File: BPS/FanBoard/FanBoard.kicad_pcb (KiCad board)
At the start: 2 copper layers, 45.1 x 33 mm, 21 parts, among them Q1 BUK9M34-100EX, Q2 BUK9M34-100EX, Q3 BUK9M34-100EX, Q4 BUK9M34-100EX

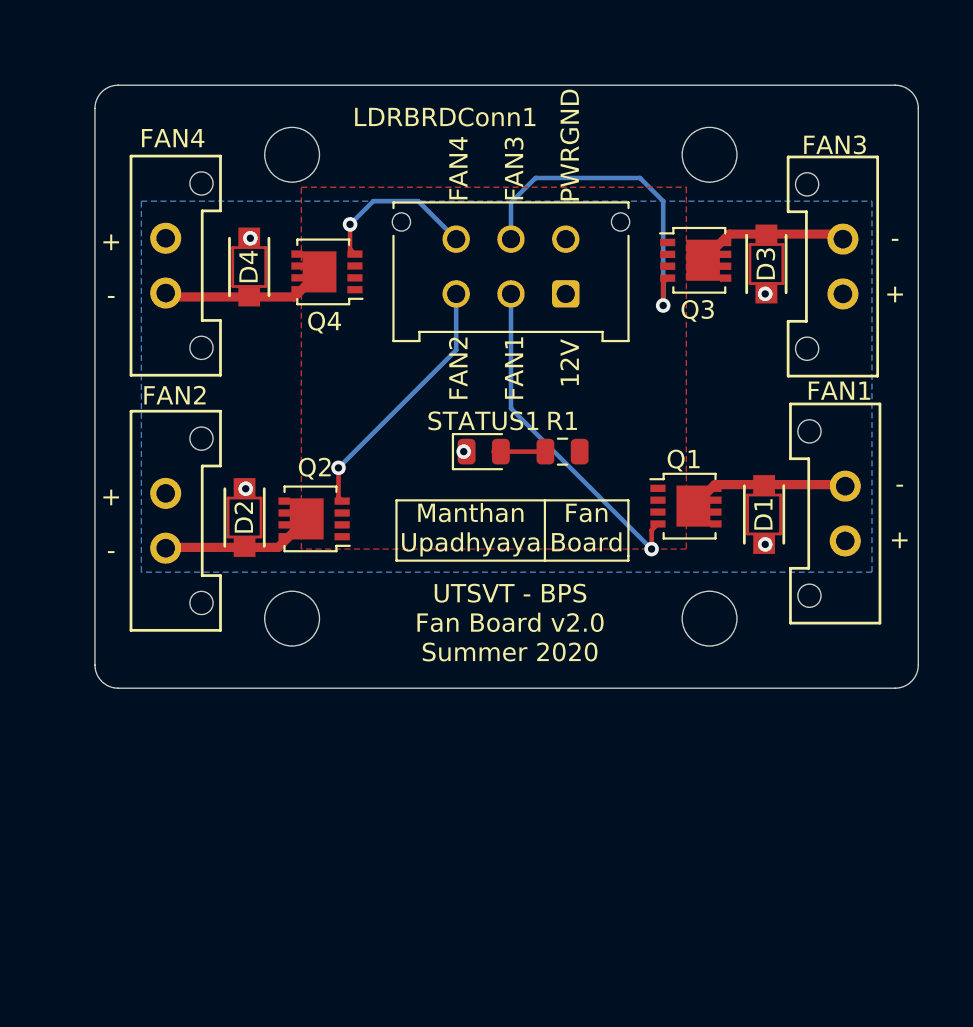
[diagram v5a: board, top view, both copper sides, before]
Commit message: Changed location of diodes and direction of status LED. Fixed value and reference labels of components, made pwrgnd plane bigger, and made distance of mounting holes on both sides symmetrical.
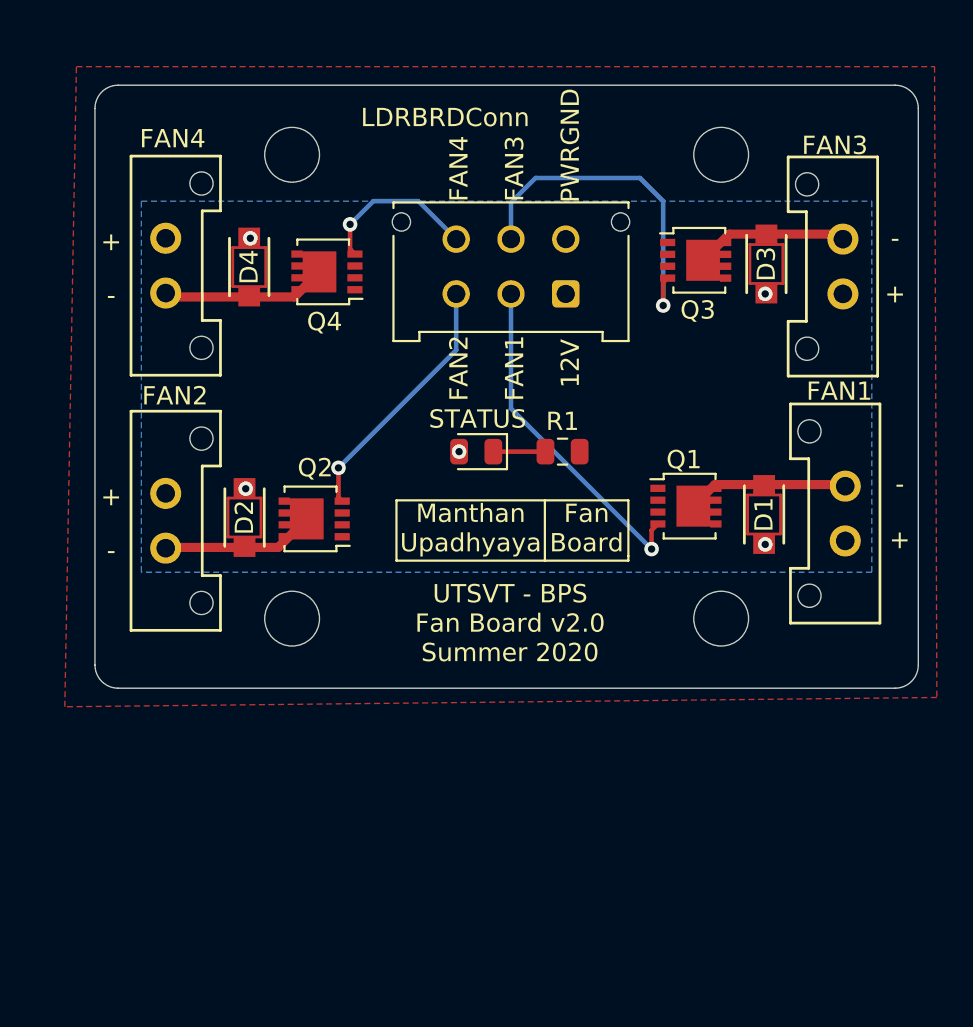
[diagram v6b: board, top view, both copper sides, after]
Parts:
- D1, D2, D3, D4: value V22F22HM3 -> V2F22HM
- FAN1: value Conn_01x02 -> FAN1
- FAN2: value Conn_01x02 -> FAN2
- FAN3: value Conn_01x02 -> FAN3
- FAN4: value Conn_01x02 -> FAN4
- LDRBRDConn: renamed from LDRBRDConn1; value Conn_02x03 -> LDRBRDConn
- moved H3 0.63 mm to (169.5, 59.7)
- moved H4 0.63 mm to (169.5, 85.1)
- moved STATUS 0.41 mm to (156.1, 75.9), turned to 180 degrees
- renumbered STATUS1 to STATUS
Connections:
- STATUS pad 1: +12V -> Net-(R1-Pad1)
- STATUS pad 2: Net-(R1-Pad1) -> +12V
